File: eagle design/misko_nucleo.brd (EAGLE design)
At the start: 115 x 73 mm, 98 parts, among them CN1 LiPo Battery, IC101 ADXL345, IC102 74HCT1G32GW, IC2 TPS63031, IC3 FT230XS, IC4 RN4678_BT_MODULE, IC6 MAX6818, IC7 SP3012-04UTG, Q2 BSS84, SW1 MICROJOYSTICK, SW2 PB6156RSL, SW3 PB6156RSL, U1 SN74LVC1G3157DBVR - BT switch, U2 ATMEGA1281-16AU, U4 MCP73871-2AAI/ML, U5 SN74LVC1G3157DBVR - GPS switch, X1 FH12-30S-0.5SH

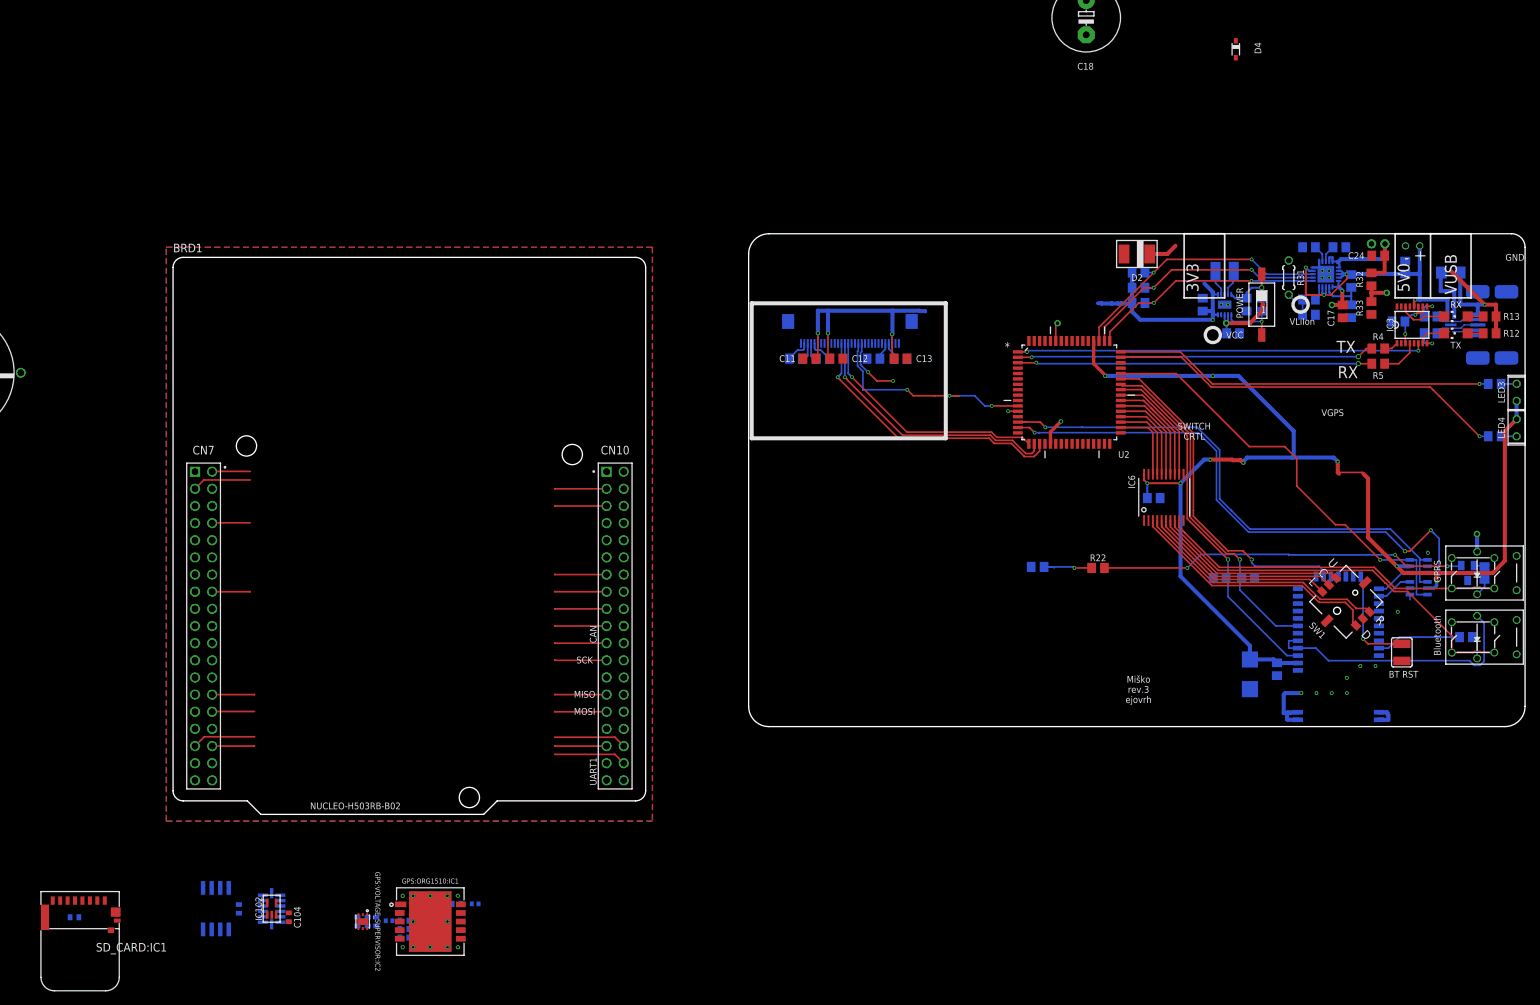
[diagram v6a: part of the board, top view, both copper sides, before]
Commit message: in misko.ioc/main.c/.h & sch/brd: - added yellow LED, defined GPIO, placed components roughly on brd
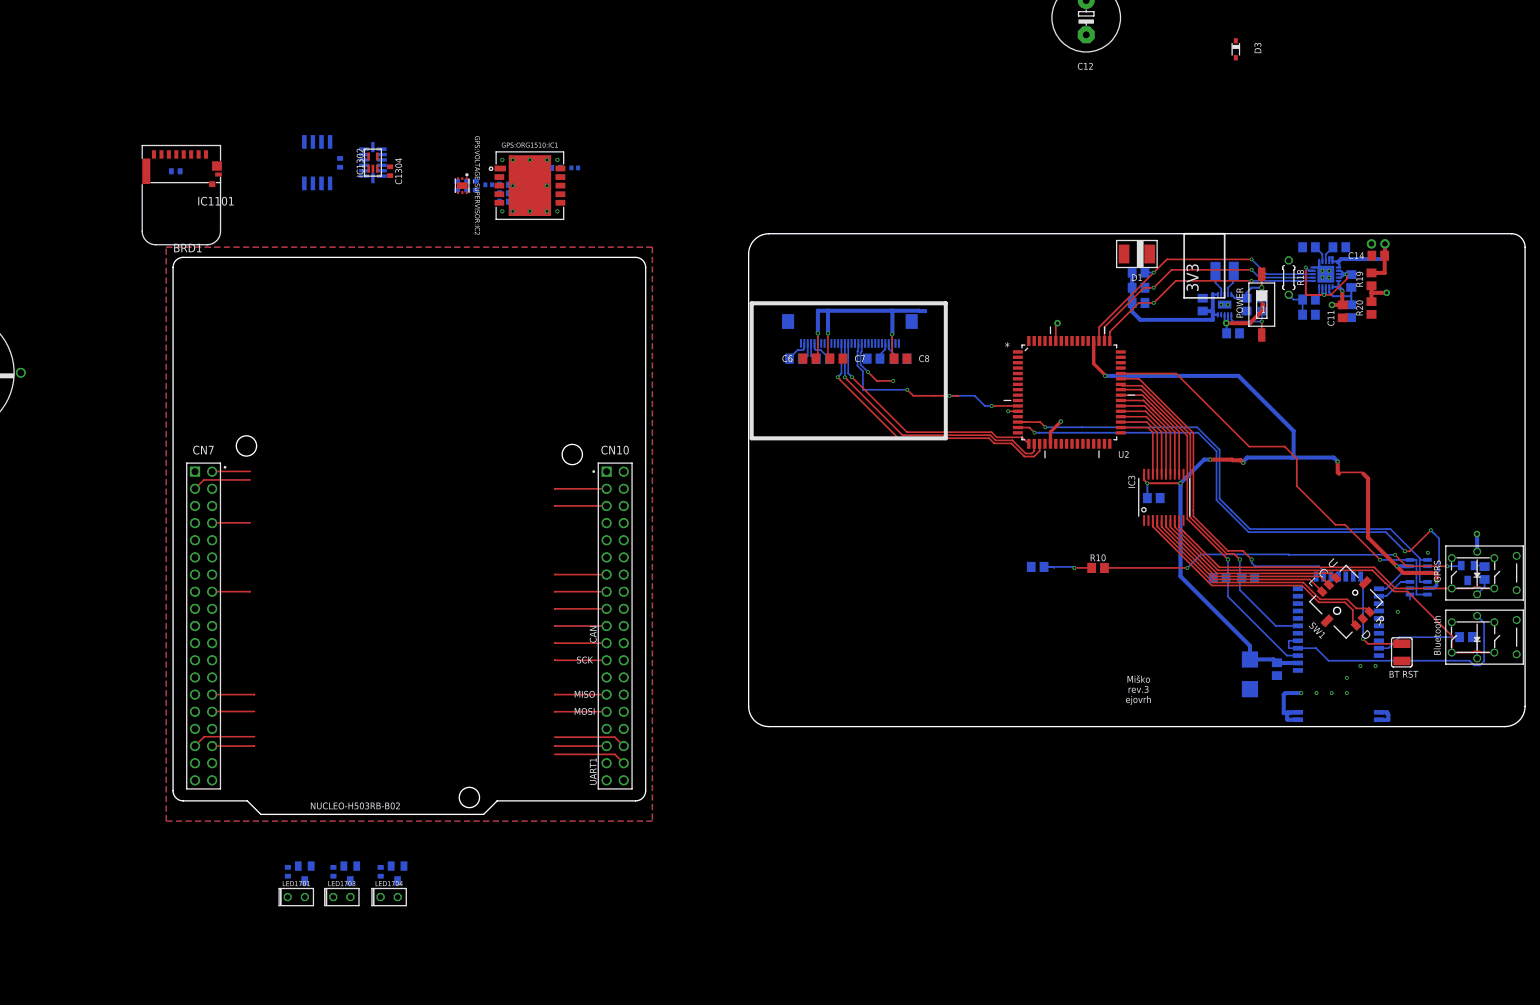
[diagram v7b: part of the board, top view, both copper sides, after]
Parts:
- removed C104, FERAM:C1, SD_CARD:C31: 0.1u / 16V, rcl:C0402
- removed C15, C22: 10µF, rcl:C0805
- removed C17, C24: 10µF, resistor:C0805
- removed C18: 1000µF, rcl:E5-10,5
- removed C27: 0.1µF, resistor:C0805
- removed CONN1: USB mini B, MX-67503-1230 USB Mini-B SMT straight socket:SMT
- removed D4: BAT60AE6327, diode:SOD323_ST
- removed F1: PTS120615V050, SparkFun-Fuses:1206
- removed FERAM:IC1: FM25W256, FM25W256 FERAM:SOIC08
- removed IC101: ADXL345, ADXL345 Accelerometer:LGA14
- removed IC102: 74HCT1G32GW, 74HCT1G32GW - OR Gate:SOT353/5
- removed IC4: RN4678_BT_MODULE, RN4678 Bluetooth 4.2 Dual Mode:SMT
- removed IC6: MAX6818, MAX6818 CMOS Switch debouncer:TSSOP20
- removed IC7: SP3012-04UTG, SP3012 TVS Diode Array:μDFN-10
- removed LED1: TX, led:CHIPLED_1206
- removed LED2: RX, led:CHIPLED_1206
- removed LED3: green, led:LED2X5
- removed LED4: red, led:LED2X5
- removed R21, R22, R24, R25: 10k, resistor:R0805
- removed R23: 1k, resistor:R0805
- removed R27, R28: 1k, rcl:R0805
- removed R29: 100k, rcl:R0805
- removed R30: 270k, rcl:R0805
- removed R31: NTC 10k, rcl:0204/5
- removed R32, R33: 150k, rcl:R0805
- removed SD_CARD:IC1: 47309-2651, Molex SD-47309 SD Card Slot:MICRO_SD_CONNECTOR
- removed U5: SN74LVC1G3157DBVR - GPS switch, Texas Instruments_By_element14_Batch_1:SOT95P280X145-6N
- added C1: 10µF, rcl:C0805
- added C1131, C1201, C1304: 0.1u / 16V, rcl:C0402
- added C2: 0.1µF, rcl:C0805
- added C5: 22µF, rcl:C0805
- added C9: 2.2µF / 25V, rcl:C0805
- added D1: BZG05C3V6-E3-TR3, zener:DO-214
- added IC1: TPS63031, TPS63031 - Buck Boost Voltage Regulator:SMT
- added IC1101: 47309-2651, Molex SD-47309 SD Card Slot:MICRO_SD_CONNECTOR
- added IC1201: FM25W256, FM25W256 FERAM:SOIC08
- added IC1301: ADXL345, ADXL345 Accelerometer:LGA14
- added IC1302: 74HCT1G32GW, 74HCT1G32GW - OR Gate:SOT353/5
- added LED1701: WP710A10SEC, led:LED2X5
- added LED1703: WP710A10LZGCK, led:LED2X5
- added LED1704: WP710A10SECK/J3, led:LED2X5
- added Q1701, Q1702, Q1703: SQ2310ES-T1_BE3, transistor-small-signal:SOT23
- added R1: 10k, resistor:R0805
- added R1701: 55R, rcl:R0402
- added R1702: 65R, rcl:R0402
- added R1703: 33R, rcl:R0402
- added R3: 270k, rcl:R0805
- added R7: 47k, rcl:R0805
- added R8: 390k, rcl:R0805
- added U3: MCP73871-2AAI/ML, MCP73871 - Powerpath and Charge Controller:QFN50P400X400X100-21N
- C10: value 0.1µF -> 10µF; device resistor:C0805 -> rcl:C0805
- C11: value 1µF -> 10µF; device rcl:C0805 -> resistor:C0805
- C12: value 1µF -> 1000µF; device rcl:C0805 -> rcl:E5-10,5
- C14: value 2.2µF / 25V -> 10µF; device rcl:C0805 -> resistor:C0805
- C3: value 10µF -> 1µF
- C4: value 0.1µF -> 1µF
- C8: value 22µF -> 10µF
- D2: value BZG05C3V6-E3-TR3 -> SZ1SMB5916BT3G; device zener:DO-214 -> diode:SMB
- D3: value SZ1SMB5916BT3G -> BAT60AE6327; device diode:SMB -> diode:SOD323_ST
- IC2: value TPS63031 -> RN4678_BT_MODULE; device TPS63031 - Buck Boost Voltage Regulator:SMT -> RN4678 Bluetooth 4.2 Dual Mode:SMT
- IC3: value FT230XS -> MAX6818; device ftdichip:SSOP16 -> MAX6818 CMOS Switch debouncer:TSSOP20
- R10: value 100k -> 10k; device rcl:R0805 -> resistor:R0805
- R11: value 270k -> 1k; device rcl:R0805 -> resistor:R0805
- R12, R13: value 1k -> 10k
- R14: value 47k -> 1k
- R16: value 1k -> 100k
- R17: value 47k -> 270k
- R18: value 1k -> NTC 10k; device resistor:R0805 -> rcl:0204/5
- R19: value 47k -> 150k
- R2: value 10k -> 100k; device resistor:R0805 -> rcl:R0805
- R20: value 390k -> 150k
- R4, R5: value 3k3 -> 47k
- R6: value 27 -> 1k
- R9: value 27 -> 10k
- U4: value MCP73871-2AAI/ML -> SN74LVC1G3157DBVR - GPS switch; device MCP73871 - Powerpath and Charge Controller:QFN50P400X400X100-21N -> Texas Instruments_By_element14_Batch_1:SOT95P280X145-6N
- moved GPS:ORG1510:C1 110.0 mm to (49.0, 90.8)
- moved GPS:ORG1510:C2 110.0 mm to (49.0, 92.0)
- moved GPS:ORG1510:C22 110.0 mm to (49.0, 93.2)
- moved GPS:ORG1510:C31 110.0 mm to (56.8, 95.8)
- moved GPS:ORG1510:IC1 110.0 mm to (52.9, 93.1)
- moved GPS:ORG1510:R1 110.0 mm to (46.8, 93.2)
- moved GPS:ORG1510:R2 110.0 mm to (59.5, 95.8)
- moved GPS:VOLTAGE_SUPERVISOR:C1 110.0 mm to (42.1, 93.1)
- moved GPS:VOLTAGE_SUPERVISOR:C2 110.0 mm to (43.6, 93.1)
- moved GPS:VOLTAGE_SUPERVISOR:IC2 110.0 mm to (42.8, 93.1)
- moved GPS:VOLTAGE_SUPERVISOR:R18 110.0 mm to (44.8, 93.1)
- moved D3 92.6 mm to (157.4, 113.3), flipped to the top
- moved C11 79.3 mm to (173.2, 74.5), turned to 270 degrees
- moved R20 74.1 mm to (177.5, 75.0), flipped to the top, turned to 270 degrees
- moved C14 72.4 mm to (178.5, 82.8), flipped to the top, turned to 180 degrees
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- renumbered Q2 to Q1, S2 to S1
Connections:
- net PC13 renamed GPS_YELLOW_LED
- removed net CBUS1: IC3.14, LED2.C
- removed net CBUS2: IC3.7, LED1.C
- removed net D+: CONN1.D+, IC7.4
- removed net D-: CONN1.D-, IC7.2
- removed net GPS_GREEN_LED: BRD1.CN7_2
- removed net GPS_RED_LED: BRD1.CN7_3
- removed net GREEN_LED: LED3.K, R15.2
- removed net ID: CONN1.ID, IC7.5
- removed net N$10: C10.1, IC3.10, IC3.11, IC3.3
- removed net N$4: F1.2, IC7.1
- removed net PC0: BRD1.CN7_38
- removed net RED_LED: LED4.K, R16.2
- removed net RXD: IC3.4, R5.2
- removed net TXD: IC3.1, R4.2
- removed net USBDM: IC3.9, R9.1
- removed net USBDP: IC3.8, R6.2
- removed net USB_D+: IC7.7, R6.1
- removed net USB_D-: IC7.9, R9.2
- removed net USB_ID: IC7.6
- removed net USB_RX_LED: LED1.A, R12.2
- removed net USB_TX_LED: LED2.A, R13.2
- removed net VUSB: CONN1.VBUS, F1.1, R12.1, R13.1
- new net LED:G_A: LED1703.A, Q1701.3
- new net LED:G_C: LED1703.K, R1703.1
- new net LED:R_A: LED1704.A, Q1702.3
- new net LED:R_C: LED1704.K, R1701.1
- new net LED:Y_A: LED1701.A, Q1703.3
- new net LED:Y_C: LED1701.K, R1702.1
- new net LED_GREEN: BRD1.CN7_2, Q1701.1
- new net LED_RED: BRD1.CN7_3, Q1702.1
- new net LED_YELLOW: BRD1.CN7_38, Q1703.1
- net 3V3: now also C1131.1, C1201.1, C1304.1, IC1101.DET, IC1101.VDD, IC1201.!HOLD!, IC1201.!WP!, IC1201.VCC, IC1301.VCC, IC1301.VDD, IC1302.VCC, R1701.2, R1702.2, R1703.2; no longer C104.1, FERAM:C1.1, FERAM:IC1.!HOLD!, FERAM:IC1.!WP!, FERAM:IC1.VCC, IC101.VCC, IC101.VDD, IC102.VCC, SD_CARD:C31.1, SD_CARD:IC1.DET, SD_CARD:IC1.VDD
- net ADXL345:ADXL345SDA: now also IC1301.SDA, IC1302.Y; no longer IC101.SDA, IC102.Y
- net ADXL345:ADXL345_INT2: now also IC1301.INT2; no longer IC101.INT2
- net ADXL345_CS: now also IC1301.!CS!, IC1302.A; no longer IC101.!CS!, IC102.A
- net ADXL345_INT1: now also IC1301.INT1; no longer IC101.INT1
- net ANALOG_SW_CTRL_PIN: now also U4.6; no longer U5.6
- net BAT_A_PIN: now also R19.2, R20.1; no longer R32.2, R33.1
- net BLUETOOTH_PROF_IND_PIN: now also IC2.P0_5; no longer IC4.P0_5
- net BLUETOOTH_RX: now also IC2.RXD; no longer IC4.RXD
- net BLUETOOTH_SWITCH_PIN: now also IC2.SW_BTN, R13.2; no longer IC4.SW_BTN, R25.2
- net BLUETOOTH_TX: now also IC2.TXD, U4.3; no longer IC4.TXD, U5.3
- net BLUETOOTH_WAKEUP_PIN: now also IC2.WAKEUP, R12.2; no longer IC4.WAKEUP, R24.2
- net BT_LED: now also IC2.LED, R6.1; no longer IC4.LED, R18.1
- net BUTTON_BLUETOOTH: now also IC3.IN7; no longer IC6.IN7
- net BUTTON_CENTER: now also IC3.IN5; no longer IC6.IN5
- net BUTTON_DOWN: now also IC3.IN2; no longer IC6.IN2
- net BUTTON_GPRS: now also IC3.IN8; no longer IC6.IN8
- net BUTTON_LEFT: now also IC3.IN4; no longer IC6.IN4
- net BUTTON_RIGHT: now also IC3.IN3; no longer IC6.IN3
- net BUTTON_UP: now also IC3.IN6; no longer IC6.IN6
- net CAP1N: now also C3.1; no longer C6.1
- net CAP1P: now also C3.2; no longer C6.2
- net CAP2N: now also C4.1; no longer C7.1
- net CAP2P: now also C4.2; no longer C7.2
- net EN: now also IC1.6_EN, R1.2; no longer IC2.6_EN, R2.2
- net GND: now also C1.1, C11.2, C1131.2, C12.-, C1201.2, C13.2, C1304.2, C14.2, C2.2, C5.1, C6.1, C7.1, C9.1, D1.AN, D2.A, IC1.3_PGND, IC1.9_GND1, IC1.GND2, IC1.GND3, IC1.GND4, IC1101.GND1, IC1101.GND2, IC1101.GND3, IC1201.GND, IC1301.GND1, IC1301.GND2, IC1301.GND3, IC1302.GND, IC2.GND, IC2.GND1, IC2.GND10, IC2.GND11, IC2.GND12, IC2.GND5, IC2.GND6, IC2.GND7, IC2.GND8, IC2.GND9, IC3.!EN!, IC3.GND, Q1701.2, Q1702.2, Q1703.2, R1.1, R12.1, R13.1, R15.2, R16.2, R17.2, R18.2, R20.2, R3.2, R8.1, R9.2, U3.10_GND1, U3.11_GND2, U3.GND2, U3.GND3, U3.GND4, U3.GND5, U3.GND6, U4.2; no longer C104.2, C11.1, C12.1, C13.1, C14.1, C15.2, C17.2, C18.-, C22.2, C24.2, C27.1, C3.1, C4.2, CONN1.GND1, CONN1.GND2, CONN1.GND3, CONN1.GND4, CONN1.GND5, D2.AN, D3.A, FERAM:C1.2, FERAM:IC1.GND, IC101.GND1, IC101.GND2, IC101.GND3, IC102.GND, IC2.3_PGND, IC2.9_GND1, IC3.13, IC3.5, IC4.GND, IC4.GND1, IC4.GND10, IC4.GND11, IC4.GND12, IC4.GND2, IC4.GND3, IC4.GND4, IC4.GND5, IC4.GND6, IC4.GND7, IC4.GND8, IC4.GND9, IC6.!EN!, IC6.GND, IC7.3, R11.2, R2.1, R20.1, R21.2, R24.1, R25.1, R28.2, R29.2, R30.2, R31.2, R33.2, SD_CARD:C31.2, SD_CARD:IC1.GND1, SD_CARD:IC1.GND2, SD_CARD:IC1.GND3, U4.10_GND1, U4.11_GND2, U4.GND2, U4.GND3, U4.GND4, U4.GND5, U4.GND6, U5.2
- net GPRS_NETLIGHT: now also R10.1, R9.1; no longer R21.1, R22.1
- net GPRS_NETLIGHT_GATE: now also R10.2; no longer R22.2
- net GPS_GREEN_LED_PIN: no longer R15.1
- net GPS_MCU_TX: now also U4.1; no longer U5.1
- net GPS_RED_LED_PIN: no longer R16.1
- net GPS_SW_SERIAL_RX: now also U4.4; no longer U5.4
- net IREF: now also R8.2; no longer R20.2
- net L2: now also R6.2; no longer R18.2
- net LDO18_O: now also IC2.LDO18_O; no longer IC4.LDO18_O
- net LDO33_O: now also IC2.LDO33_O, IC2.VDD_IO; no longer IC4.LDO33_O, IC4.VDD_IO
- net L_L1: now also IC1.4_L1; no longer IC2.4_L1
- net L_L2: now also IC1.2_L2; no longer IC2.2_L2
- net MCP73871_CHARGE_STATUS_1_PIN: now also R7.2, U3.8_STAT1; no longer R19.2, U4.8_STAT1
- net MCP73871_CHARGE_STATUS_2_PIN: now also R5.2, U3.7_STAT2; no longer R17.2, U4.7_STAT2
- net MCP73871_POWER_GOOD_PIN: now also R4.2, U3.!6_PG!; no longer R14.2, U4.!6_PG!
- net MENU_BLUETOOTH_POWER_BUTTON_PIN: now also IC3.OUT7; no longer IC6.OUT7
- net MENU_CENTER_BUTTON_PIN: now also IC3.OUT5; no longer IC6.OUT5
- net MENU_DOWN_BUTTON_PIN: now also IC3.OUT2; no longer IC6.OUT2
- net MENU_GPRS_POWER_BUTTON_PIN: now also IC3.OUT8; no longer IC6.OUT8
- net MENU_LEFT_BUTTON_PIN: now also IC3.OUT4; no longer IC6.OUT4
- net MENU_RIGHT_BUTTON_PIN: now also IC3.OUT3; no longer IC6.OUT3
- net MENU_UP_BUTTON_PIN: now also IC3.OUT6; no longer IC6.OUT6
- net N$1: now also R11.1; no longer R23.1
- net N$11: now also IC2.!RST_N!; no longer IC4.!RST_N!
- net N$19: now also R14.2, R17.1, R18.1; no longer R27.2, R30.1, R31.1
- net N$3: now also R11.2; no longer R23.2
- net N$6: now also C12.+, D3.C; no longer C18.+, D4.C
- net OLD_5V0: now also D3.A, R2.1, U3.17_CE, U3.18_IN1, U3.19_IN2, U3.3_SEL, U3.4_PROG2, U3.9_!TE!; no longer C27.2, D4.A, IC3.12, IC7.10, R10.1, U4.17_CE, U4.18_IN1, U4.19_IN2, U4.3_SEL, U4.4_PROG2, U4.9_!TE!
- net PDI_UART0_CTS_PIN: no longer IC3.6
- net PDI_UART0_RX_PIN: no longer R4.1
- net PDI_UART0_TX_PIN: no longer R5.1
- net PROG1: now also R15.1, U3.13_PROG1; no longer R28.1, U4.13_PROG1
- net PROG3: now also R16.1, U3.12_PROG3; no longer R29.1, U4.12_PROG3
- net SD_CD: now also IC1101.POL; no longer SD_CARD:IC1.POL
- net SPI1_FRAM_CS: now also IC1201.!CS!; no longer FERAM:IC1.!CS!
- net SPI1_MISO: now also IC1101.CMD, IC1101.DAT0, IC1201.SO, IC1301.SDO; no longer FERAM:IC1.SO, IC101.SDO, SD_CARD:IC1.CMD, SD_CARD:IC1.DAT0
- net SPI1_MOSI: now also IC1201.SI, IC1302.B; no longer FERAM:IC1.SI, IC102.B
- net SPI1_SCK: now also IC1101.CLK, IC1201.SCK, IC1301.SCL; no longer FERAM:IC1.SCK, IC101.SCL, SD_CARD:IC1.CLK
- net SPI1_SD_CS: now also IC1101.CD/DAT3; no longer SD_CARD:IC1.CD/DAT3
- net THERM: now also R14.1, U3.5_THERM; no longer R27.1, U4.5_THERM
- net VCC: now also C10.1, C13.1, C5.2, C6.2, C7.2, D1.CAT, D2.C, IC1.10_FB, IC1.1_VOUT, IC2.BAT_IN, IC3.VCC, R4.1, R5.1, R7.1, U4.5; no longer C11.2, C12.2, C13.2, C15.1, C22.1, D2.CAT, D3.C, IC2.10_FB, IC2.1_VOUT, IC4.BAT_IN, IC6.VCC, LED3.A, LED4.A, R14.1, R17.1, R19.1, U5.5
- net VCOMH: now also C9.2; no longer C14.2
- net VPCC: now also R2.2, R3.1, U3.2_VPCC; no longer R10.2, R11.1, U4.2_VPCC
- net V_LIION+: now also C14.1, R19.1, U3.14_VBAT1, U3.15_VBAT2, U3.16_BAT_SENSE; no longer C24.1, R32.1, U4.14_VBAT1, U4.15_VBAT2, U4.16_BAT_SENSE
- net V_LIION_REGULATED: now also C1.2, C11.1, C2.1, IC1.5_VIN, IC1.7_PS/SYNC, IC1.8_VINA, U3.1_OUT1, U3.20_OUT2; no longer C17.1, C3.2, C4.1, IC2.5_VIN, IC2.7_PS/SYNC, IC2.8_VINA, U4.1_OUT1, U4.20_OUT2
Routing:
- net PDI_UART0_CTS_PIN: track 60.5 -> 0.00 mm, vias 2 -> 0
- net GPS_RED_LED_PIN: track 59.3 -> 0.00 mm, vias 1 -> 0
- net GPS_GREEN_LED_PIN: track 56.4 -> 0.00 mm, vias 1 -> 0
- net PDI_UART0_RX_PIN: track 53.0 -> 0.00 mm, vias 2 -> 0
- net PDI_UART0_TX_PIN: track 52.5 -> 0.00 mm, vias 2 -> 0
- net VCC: track 265.7 -> 219.0 mm, vias 14 -> 12
- net OLD_5V0: track 46.4 -> 19.7 mm, vias 5 -> 3
- net VUSB: track 22.8 -> 0.00 mm, vias 1 -> 0
- net N$10: track 8.99 -> 0.00 mm, vias 2 -> 0
- net N$4: track 8.85 -> 0.00 mm
- net LED_RED: track 0.00 -> 8.72 mm
- net GPS_RED_LED: track 8.72 -> 0.00 mm
- net CBUS1: track 7.65 -> 0.00 mm
- net RXD: track 5.80 -> 0.00 mm
- net LED_GREEN: track 0.00 -> 5.66 mm
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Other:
- board text removed: "+"
- board text removed: "-"
- board text removed: "5V0"
- board text removed: "GND"
- board text removed: "RX"
- board text removed: "SWITCH CRTL"
- board text removed: "TX"
- board text removed: "VCC"
- board text removed: "VGPS"
- board text removed: "VLiIon"
- board text removed: "VUSB"

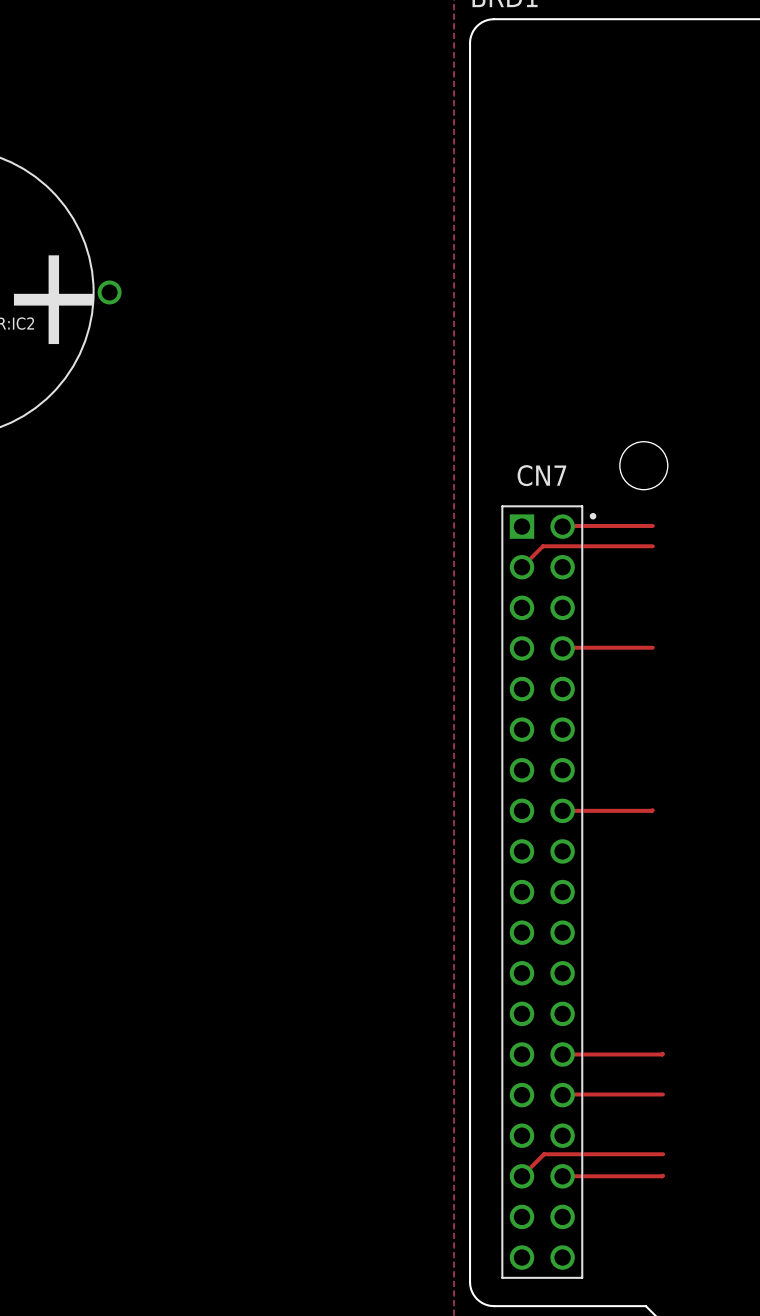
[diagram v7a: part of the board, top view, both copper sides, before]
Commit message: in brd & sch/misko.ioc/main.c/.h: - added support for a supercap discharge FET/resistor circuit
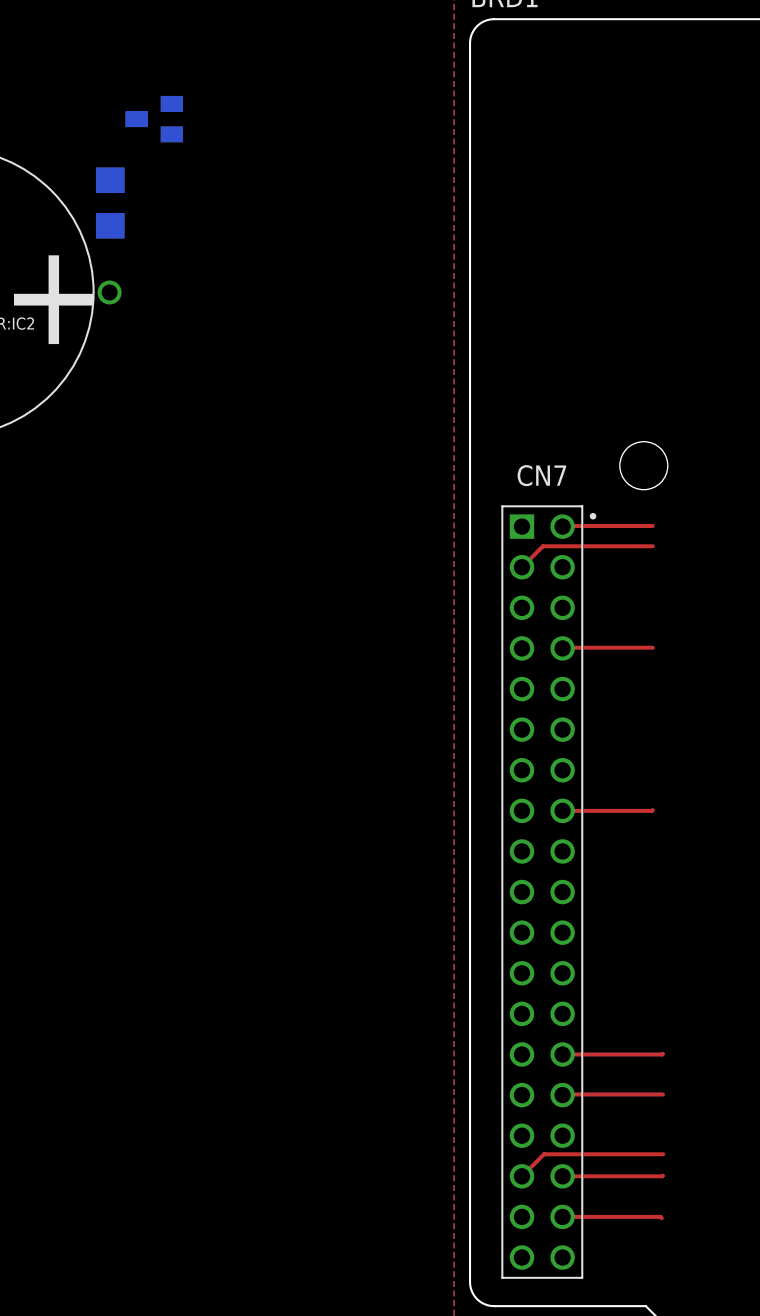
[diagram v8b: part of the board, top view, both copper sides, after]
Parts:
- added GPS:SUPERCAP+CHARGER:Q4: SQ2310ES-T1_BE3, transistor-small-signal:SOT23
- added GPS:SUPERCAP+CHARGER:R1: 33R, resistor:R1206
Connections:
- removed net PC1: BRD1.CN7_36
- new net GPS:SUPERCAP+CHARGER:N$1: GPS:SUPERCAP+CHARGER:Q4.3, GPS:SUPERCAP+CHARGER:R1.1
- new net SUPERCAP_DISCHARGE: BRD1.CN7_36, GPS:SUPERCAP+CHARGER:Q4.1
- net GND: now also GPS:SUPERCAP+CHARGER:Q4.2
- net GPS:VGPS: now also GPS:SUPERCAP+CHARGER:R1.2
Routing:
- net SUPERCAP_DISCHARGE: track 0.00 -> 6.24 mm
